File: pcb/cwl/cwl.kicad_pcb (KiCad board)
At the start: 2 copper layers, 60.5 x 62 mm, 25 parts, among them J1 UEXT, J2 OpenTherm, J3 OLED_SH1106, J4 EXT_GPIO, J5 AUX, Q1 2N7002, SW1 EC12E24204A9, U1 LTV-817S-B, U2 LTV-817S-B

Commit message: pcb
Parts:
- removed MH3: M3, MountingHole:MountingHole_3.2mm_M3_Pad_Via
- added D4: 1N4148WS, Diode_SMD:D_SOD-323, F.Cu at (123.7, 50.2)
- added D5: 1N4148WS, Diode_SMD:D_SOD-323, F.Cu at (125.7, 50.2)
- added SB1: GPIO4→OT_TX, Jumper:SolderJumper-2_P1.3mm_Open_RoundedPad1.0x1.5mm, B.Cu at (93.1, 56.5)
- added SB2: GPIO36→OT_RX, Jumper:SolderJumper-2_P1.3mm_Open_RoundedPad1.0x1.5mm, B.Cu at (93.1, 59.0)
- added SB3: TXD→OT_TX, Jumper:SolderJumper-2_P1.3mm_Bridged_RoundedPad1.0x1.5mm, B.Cu at (88.6, 56.5)
- added SB4: RXD→OT_RX, Jumper:SolderJumper-2_P1.3mm_Bridged_RoundedPad1.0x1.5mm, B.Cu at (88.6, 59.0)
- D1: value BZX384-C3V3 -> BZX384-C4V7
- J1, J2, J4, J5, R6, R7: moved to B.Cu
- moved J4 76.3 mm to (114.9, 44.5), turned to 180 degrees
- moved LED1 74.7 mm to (74.6, 72.3)
- moved J1 70.9 mm to (81.3, 45.0), turned to -90 degrees
- moved U2 64.6 mm to (122.0, 64.0), turned to 90 degrees
- moved J2 63.5 mm to (121.6, 46.8)
- moved R8 62.7 mm to (74.7, 70.3), turned to 180 degrees
- moved D3 62.5 mm to (127.7, 50.2), turned to -90 degrees
- moved D2 61.8 mm to (121.7, 50.2), turned to -90 degrees
- moved R7 60.8 mm to (104.9, 58.5)
- moved R6 60.3 mm to (104.9, 56.5)
- moved MH4 57.8 mm to (103.2, 44.0)
- moved R5 57.0 mm to (123.8, 58.4), turned to 90 degrees
- moved U1 56.6 mm to (128.7, 64.2), turned to 90 degrees
- moved SW1 55.3 mm to (102.0, 54.2)
- moved R4 53.9 mm to (120.8, 58.4), turned to 90 degrees
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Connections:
- J4 pad 1: GPIO4_OT_TX -> GPIO4
- J4 pad 2: GPIO36_OT_RX -> GPIO36
- R1 pad 1: GPIO4_OT_TX -> OT_TX_SIG
- R4 pad 1: GPIO36_OT_RX -> OT_RX_SIG
- U2 pad 4: GPIO36_OT_RX -> OT_RX_SIG
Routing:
- net GND: track 0.00 -> 215.6 mm, vias 0 -> 2
- net +3V3: track 0.00 -> 101.4 mm
- net OT_TX_SIG: track 0.00 -> 47.0 mm, vias 0 -> 1
- net ENC_SW: track 0.00 -> 45.4 mm
- net UEXT_TXD: track 0.00 -> 44.2 mm
- net UEXT_RXD: track 0.00 -> 40.3 mm
- net ENC_DT: track 0.00 -> 36.3 mm
- net GPIO4: track 0.00 -> 27.8 mm
- net ENC_CLK: track 0.00 -> 27.5 mm
- net LED_GPIO: track 0.00 -> 26.3 mm
- net SDA: track 0.00 -> 24.8 mm
- net GPIO36: track 0.00 -> 24.6 mm
- net OT+: track 0.00 -> 24.3 mm
- net SCL: track 0.00 -> 22.7 mm
- net OT-: track 0.00 -> 14.0 mm
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- added copper zone on B.Cu, net GND
- added copper zone on F.Cu, net GND
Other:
- board size 60.5 x 62 mm -> 65.5 x 34.2 mm

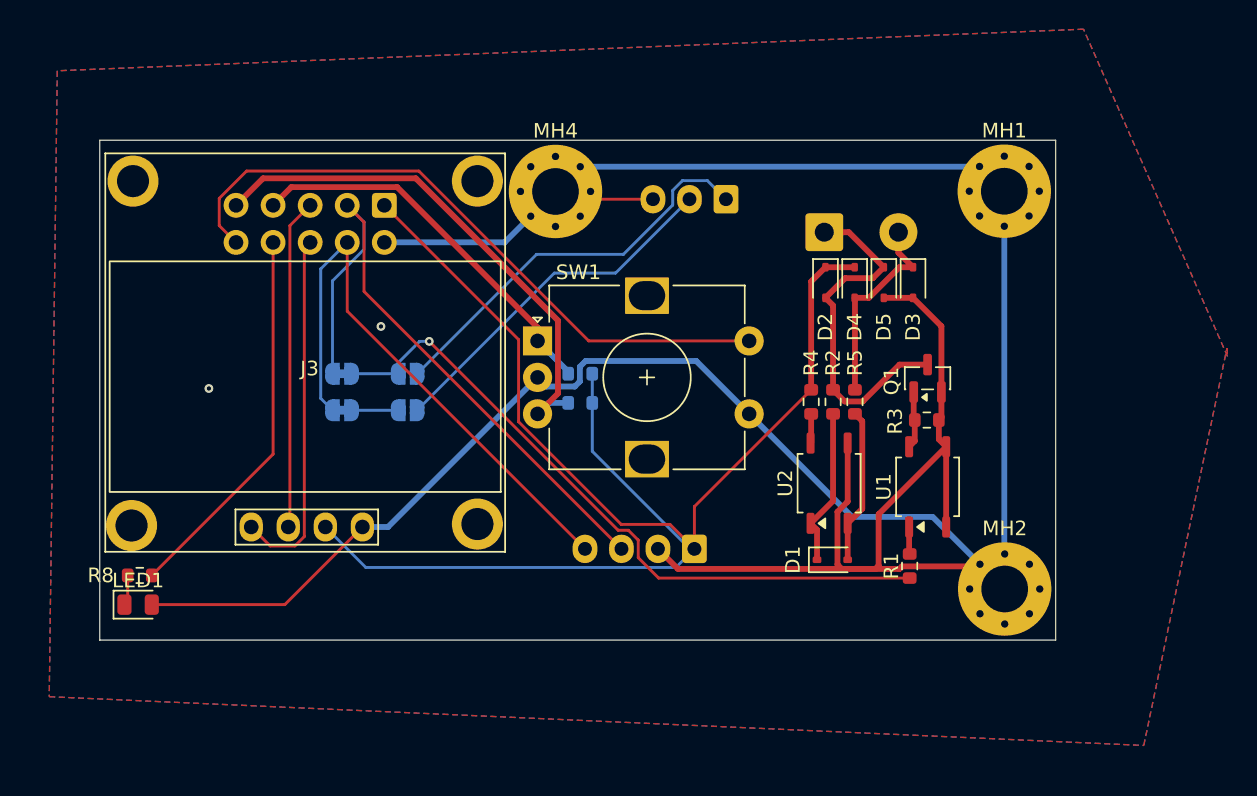
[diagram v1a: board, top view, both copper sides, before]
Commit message: update display
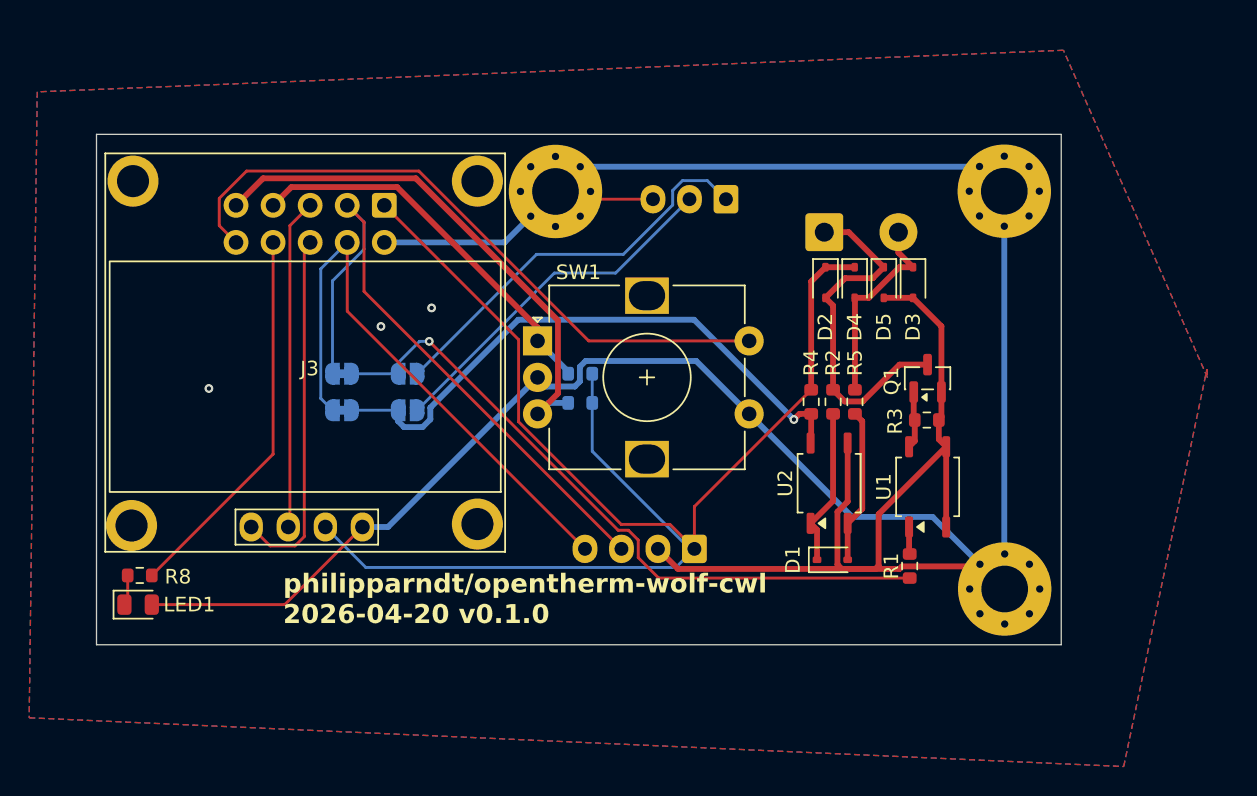
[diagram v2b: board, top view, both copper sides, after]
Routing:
- net OT_RX_SIG: track 5.22 -> 40.9 mm, vias 0 -> 1
- net GND: vias 2 -> 3
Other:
- board size 65.5 x 34.2 mm -> 66.1 x 35 mm
- board text added: "philipparndt/opentherm-wolf-cwl 2026-04-20 v0.1.0"

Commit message: generate gerber files
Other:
- board text added: "Configure"
- board text added: "J4"
- board text added: "J4 (EXT_GPIO) 1: GPIO4 (OT TX) 2: GPIO36 (OT RX) 3: GND"
- board text added: "J5 (AUX) 1: +3V3 2: GND 3: TXD 4: RXD"
- board text added: "UEXT"
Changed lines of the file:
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@@
+	)
+	(gr_rect
+		(start 83.06 52.38)
+		(end 98.69 62.92)
+		(stroke
+			(width 0.1)
+			(type default)
+		)
+		(fill no)
+		(layer "B.SilkS")
 	)
 	(gr_rect
@@
 		)
 	)
+	(gr_text "UEXT"
+		(at 90.14 62.46 0)
+		(layer "B.SilkS")
+		(effects
+			(font
+				(size 1 1)
+				(thickness 0.1)
+			)
+			(justify left bottom mirror)
+		)
+	)
+	(gr_text "J4"
+		(at 94.03 62.46 0)
+		(layer "B.SilkS")
+		(effects
+			(font
+				(size 1 1)
+				(thickness 0.1)
+			)
+			(justify left bottom mirror)
+		)
+	)
+	(gr_text "Configure"
+		(at 94.42 54.31 0)
+		(layer "B.SilkS")
+		(effects
+			(font
+				(size 1 1)
+				(thickness 0.1)
+			)
+			(justify left bottom mirror)
+		)
+	)
+	(gr_text " J5 (AUX)\n 1: +3V3\n 2: GND\n 3: TXD\n 4: RXD"
+		(at 124.94 72.88 0)
+		(layer "B.SilkS")
+		(effects
+			(font
+				(size 1 1)
+				(thickness 0.1)
+			)
+			(justify left bottom mirror)
+		)
+	)
+	(gr_text "J4 (EXT_GPIO)\n1: GPIO4 (OT TX)\n2: GPIO36 (OT RX)\n3: GND"
+		(at 135.89 61.76 0)
+		(layer "B.SilkS")
+		(effects
+			(font
+				(size 1 1)
+				(thickness 0.1)
+			)
+			(justify left bottom mirror)
+		)
+	)

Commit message: chore: archive completed changes, add cwl-1.3 PCB variant
- Archive completed OpenSpec changes under 2026-05-01:
  bypass-default, timed-off-cancel, home-header-mode,
  pending-mode-indicator, main-screen-schedule-indicator,
  rust-rewrite, ventilation-select-schedule-return
- Add new cwl-1.3 PCB variant with KiCad project files
- Add OLED SH1106 0.96" 3D model and large mounting-hole
  footprint variant
- Update PCB assembly plots, BOM, and 3D model generation
  scripts
- Refactor ESP32 firmware: display, encoder, framebuffer,
  network, scheduler, and OpenTherm master modules
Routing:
- net GND: vias 3 -> 5
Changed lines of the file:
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@@
 		)
 		(embedded_fonts no)
-		(model "/Users/philipparndt/dev/smarthome/projects/opentherm-wolf-cwl/pcb/3dmodels/OLED_SH1106_1.3inch.step"
+		(model "/Users/philipparndt/dev/smarthome/projects/opentherm-wolf-cwl/pcb/3dmodels/OLED_SH1106_0.96inch.step"
 			(offset
 				(xyz 0 0 0)
@@
 	)
 	(via
+		(at 97.43 54.06)
+		(size 0.6)
+		(drill 0.3)
+		(layers "F.Cu" "B.Cu")
+		(free yes)
+		(net "GND")
+	)
+	(via
 		(at 94.74 51.99)
 		(size 0.6)
@@
 		(size 0.6)
 		(drill 0.3)
+		(layers "F.Cu" "B.Cu")
+		(free yes)
+		(net "GND")
+	)
+	(via
+		(at 105.66 51.23)
+		(size 0.6)
+		(drill 0.3)

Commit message: new pcb
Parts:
- removed J4: EXT_GPIO, Connector_JST:JST_XH_B3B-XH-A_1x03_P2.50mm_Vertical
- removed J5: AUX, Connector_JST:JST_XH_B4B-XH-A_1x04_P2.50mm_Vertical
- removed SB1: GPIO4→OT_TX, Jumper:SolderJumper-2_P1.3mm_Open_RoundedPad1.0x1.5mm
- removed SB2: GPIO36→OT_RX, Jumper:SolderJumper-2_P1.3mm_Open_RoundedPad1.0x1.5mm
- added D6: BZT52C15, Diode_SMD:D_SOD-123, F.Cu at (125.3, 90.0)
- added D7: BZT52C4V3, Diode_SMD:D_SOD-123, F.Cu at (128.6, 90.0)
- added MH3: M3, MountingHole:MountingHole_3.2mm_M3_Pad_Via, F.Cu at (43.6, 106.4)
- D1: value BZX384-C4V7 -> 1N4148WS
- D5: value 1N4148WS -> BZT52C4V7; footprint Diode_SMD:D_SOD-323 -> Diode_SMD:D_SOD-123
- J3: value OLED_SH1106 -> OLED; footprint SSD1306:128x64OLED-MountingHoles -> SSD1306:128x64OLED-MountingHoles-Combined
- Q1: value 2N7002 -> BC858A
- R2: value 680 -> 220
- R3: value 4.7k -> 100
- R4: value 10k -> 330
- R5: value 1k -> 1.5k
- R6, R7, SB3, SB4: moved to F.Cu
- U1, U2: value LTV-817S-B -> PC817; footprint Package_SO:SOP-4_3.8x4.1mm_P2.54mm -> Package_SO:SOP-4_7.5x4.1mm_P2.54mm
- moved MH1 92.5 mm to (43.8, 64.2)
- moved MH4 69.7 mm to (135.7, 105.7)
- moved R7 65.5 mm to (45.6, 86.2), turned to 180 degrees
- moved R6 65.4 mm to (45.6, 84.0)
- moved SW1 59.2 mm to (50.2, 82.8)
- moved SB4 57.4 mm to (136.4, 90.8), turned to 90 degrees
- moved SB3 56.4 mm to (133.4, 90.8), turned to 90 degrees
- moved LED1 40.7 mm to (51.2, 105.6)
- moved R8 40.3 mm to (55.3, 105.6)
- moved D5 39.9 mm to (122.1, 90.0)
- moved R4 31.4 mm to (133.4, 87.1), turned to -90 degrees
- moved R5 31.4 mm to (136.4, 87.1)
- moved J3 27.6 mm to (72.1, 68.4), turned to 0 degrees
- moved D4 27.3 mm to (120.5, 77.3)
- moved D3 27.1 mm to (126.1, 77.3)
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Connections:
- D1 pad 1: RX_ANODE -> Net-(D1-K)
- D1 pad 2: RX_CATHODE -> OT+
- D2 pad 1: +3V3 -> Net-(D1-K)
- D2 pad 2: OT+ -> OT-
- D3 pad 1: OT- -> OT+
- D3 pad 2: GND -> Net-(D3-A)
- D4 pad 1: +3V3 -> OT-
- D4 pad 2: OT- -> Net-(D3-A)
- D5 pad 1: OT+ -> Net-(D5-K)
- D5 pad 2: GND -> Net-(D3-A)
- J2 pad 1: OT+ -> OT-
- J2 pad 2: OT- -> OT+
- J3 pad 1: GND -> +3V3
- J3 pad 2: +3V3 -> GND
- LED1 pad 1: LED_ANODE -> GND
- LED1 pad 2: GND -> Net-(LED1-A)
- Q1 pad 1: TX_GATE -> Net-(D6-K)
- Q1 pad 2: GND -> Net-(D1-K)
- Q1 pad 3: OT+ -> Net-(D5-K)
- R1 pad 1: OT_TX_SIG -> Net-(D1-K)
- R1 pad 2: TX_LED -> Net-(D6-K)
- R2 pad 1: OT+ -> Net-(R2-Pad1)
- R2 pad 2: RX_ANODE -> Net-(D5-K)
- R3 pad 1: TX_GATE -> Net-(R2-Pad1)
- R3 pad 2: GND -> Net-(D3-A)
- R4 pad 1: OT_RX_SIG -> Net-(R4-Pad1)
- R4 pad 2: +3V3 -> OT_TX_SIG
- R5 pad 1: RX_CATHODE -> OT_RX_SIG
- R5 pad 2: OT- -> GND
- R6 pad 1: ENC_CLK -> +3V3
- R6 pad 2: +3V3 -> ENC_CLK
- R8 pad 2: LED_ANODE -> Net-(LED1-A)
- U1 pad 1: TX_LED -> Net-(R4-Pad1)
- U1 pad 3: GND -> Net-(D7-K)
- U1 pad 4: TX_GATE -> Net-(D6-K)
- U2 pad 1: RX_ANODE -> Net-(R2-Pad1)
- U2 pad 2: RX_CATHODE -> Net-(D3-A)
- U2 pad 3: GND -> OT_RX_SIG
- U2 pad 4: OT_RX_SIG -> +3V3
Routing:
- net GND: track 215.6 -> 272.3 mm, vias 5 -> 3
- net Net-(D3-A): track 0.00 -> 54.6 mm
- net +3V3: track 101.4 -> 153.1 mm
- net OT_TX_SIG: track 47.0 -> 2.19 mm, vias 1 -> 0
- net GPIO4: track 27.8 -> 0.00 mm
- net LED_GPIO: track 26.3 -> 51.5 mm
- net GPIO36: track 24.6 -> 0.00 mm
- net ENC_CLK: track 27.5 -> 50.0 mm
- net Net-(D6-K): track 0.00 -> 21.6 mm
- net Net-(D7-K): track 0.00 -> 19.6 mm
- net ENC_SW: track 45.4 -> 28.1 mm
- net Net-(R2-Pad1): track 0.00 -> 16.7 mm
- net ENC_DT: track 36.3 -> 51.5 mm
- net UEXT_RXD: track 40.3 -> 55.5 mm
- net SCL: track 22.7 -> 37.6 mm
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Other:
- board size 66.1 x 35 mm -> 100 x 50 mm
- board text added: "philipparndt/opentherm-wolf-cwl 2026-05-17 v0.2.0"
- board text removed: "Configure"
- board text removed: "J4"
- board text removed: "J4 (EXT_GPIO) 1: GPIO4 (OT TX) 2: GPIO36 (OT RX) 3: GND"
- board text removed: "J5 (AUX) 1: +3V3 2: GND 3: TXD 4: RXD"
- board text removed: "UEXT"
- board text removed: "philipparndt/opentherm-wolf-cwl 2026-04-20 v0.1.0"

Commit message: new pcb
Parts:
- renumbered SB3 to SB1, SB4 to SB2
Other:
- board text added: "RoHS Compliant"
